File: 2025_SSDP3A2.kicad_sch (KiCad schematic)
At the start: 66 parts, among them J1 SolderPad, J2 SolderPad, J3 SolderPad, J4 SolderPad, Q1 CSD19534Q5A, Q2 BSC0805LS, U1 LM5146RGYR

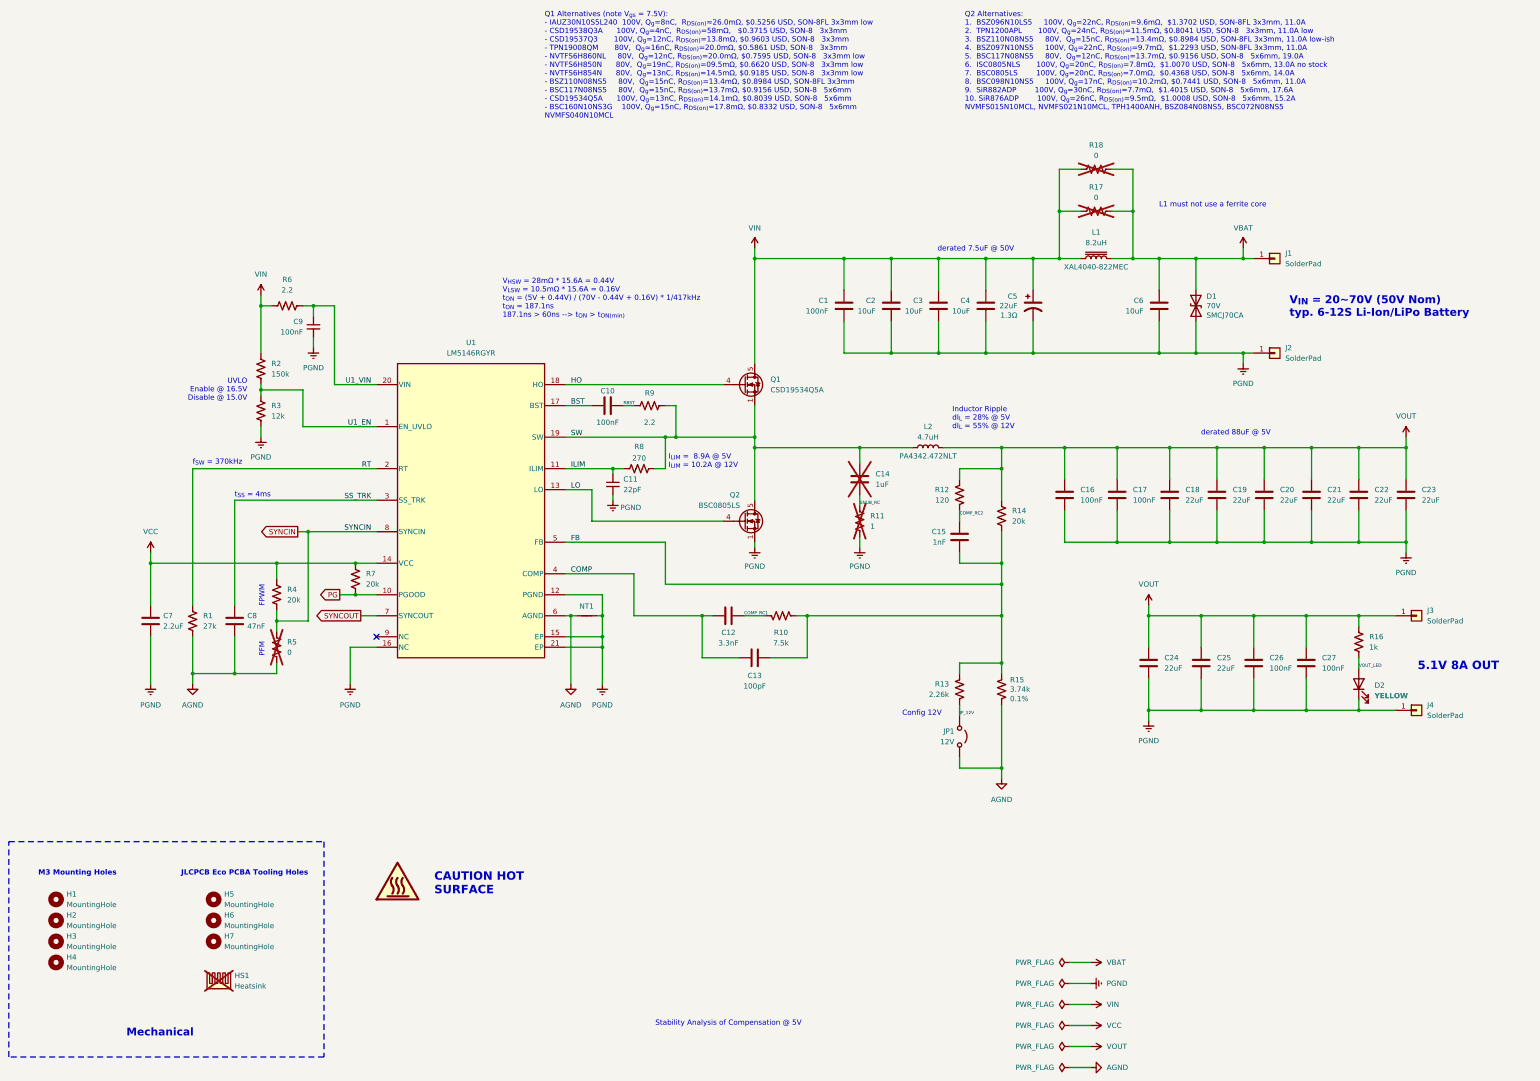
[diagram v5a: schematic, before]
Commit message: Revised PCB layout, simplified EMI filter
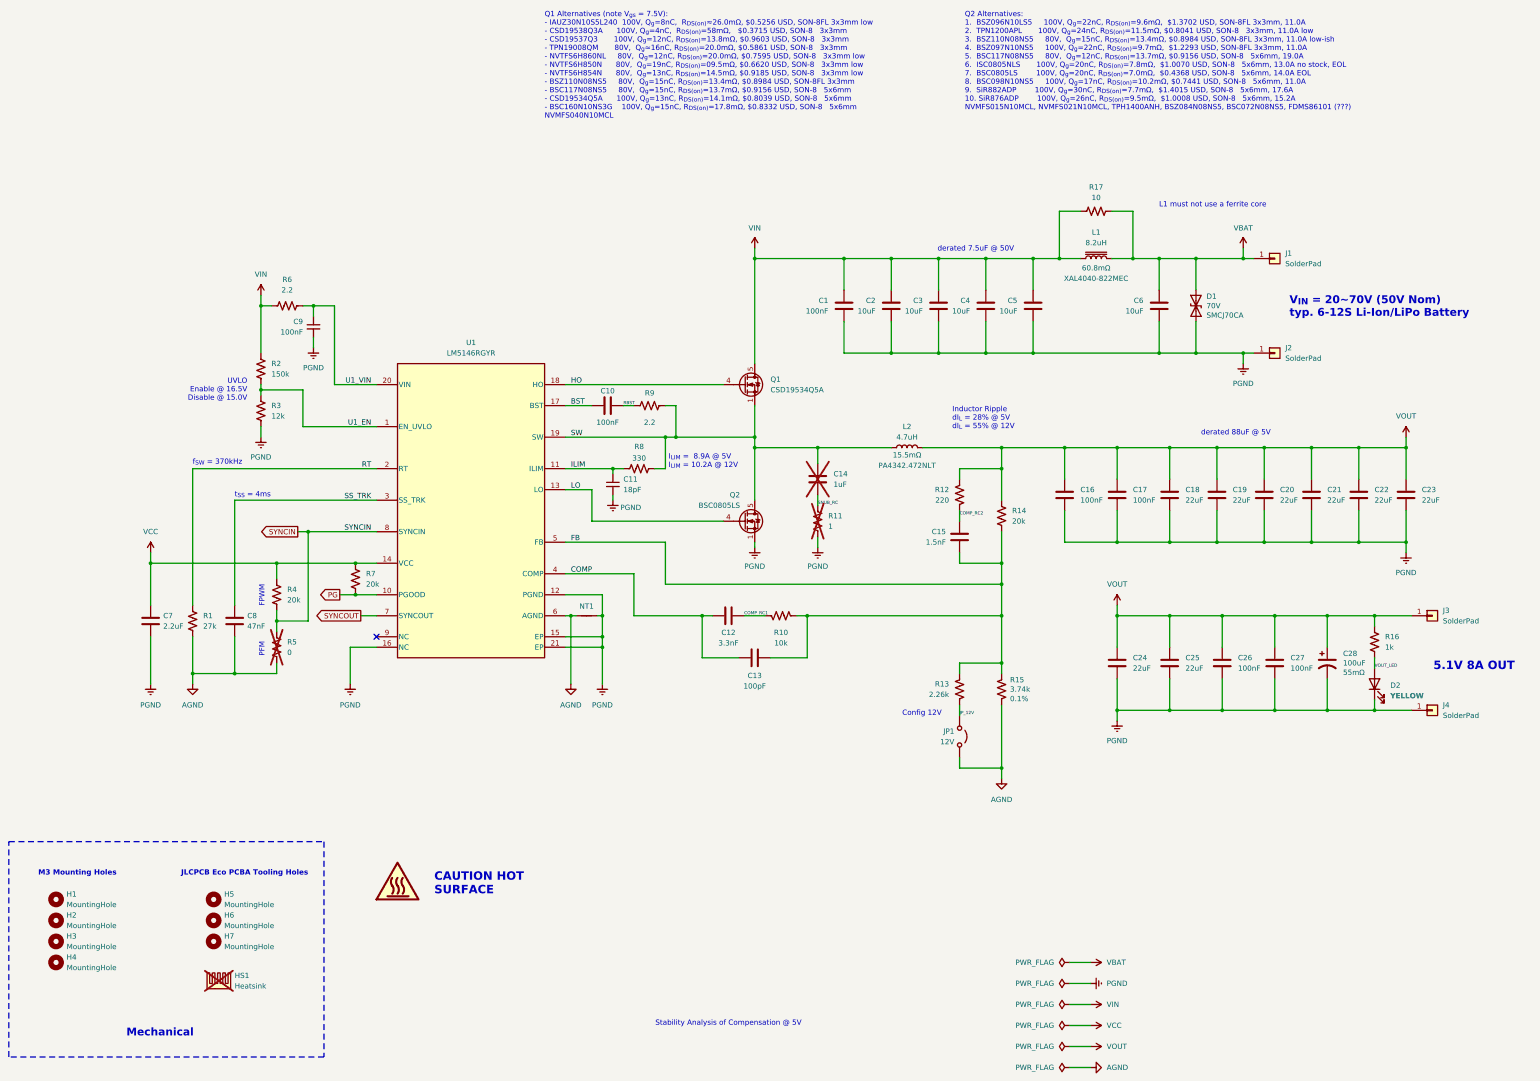
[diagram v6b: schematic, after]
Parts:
- removed C5: 22uF, Capacitor_SMD:CP_Elec_8x10.5, symbol Device:C_Polarized_US
- removed R18: 0, Resistor_SMD:R_2010_5025Metric, symbol Device:R_US
- added C28: 100uF, Capacitor_Tantalum_SMD:CP_EIA-7343-30_AVX-N_HandSolder, symbol Device:C_Polarized_US
- added C5: 10uF, Capacitor_SMD:C_1210_3225Metric, symbol Device:C
- C1, C10, C16, C17, C26, C27, C9: MANUFACTURER (none) -> YAGEO; Tolerance (none) -> 10%; Voltage (none) -> 100V
- C11: value 22pF -> 18pF; LCSC PN C408549 -> C913624; MANUFACTURER (none) -> Murata Electronics; Tolerance (none) -> 5%; Voltage (none) -> 100V
- C12, C7, C8: MANUFACTURER (none) -> Panasonic; Tolerance (none) -> 10%; Voltage (none) -> 50V
- C13: MANUFACTURER (none) -> Panasonic; Tolerance (none) -> 5%; Voltage (none) -> 50V
- C15: value 1nF -> 1.5nF; LCSC PN C1588 -> C1595; MANUFACTURER (none) -> Guangdong Fenghua; Part Type Basic -> Preferred Extended; Tolerance (none) -> 10%; Voltage (none) -> 50V
- C18, C19, C20, C21, C22, C23, C24, C25: ESR (none) -> 3.4mΩ; MANUFACTURER (none) -> Panasonic; Tolerance (none) -> 20%; Voltage (none) -> 25V
- C2, C3, C4, C6: ESR (none) -> 2mΩ; MANUFACTURER (none) -> Murata Electronics; Tolerance (none) -> 10%; Voltage (none) -> 100V
- D1: FT Rotation Offset (none) -> 0; LCSC PN (none) -> C41411746; MANUFACTURER (none) -> Zhuhai Hongjiacheng; Part Type (none) -> Preferred Extended; Voltage (none) -> 113V
- D2: MANUFACTURER (none) -> Hubei KENTO Electronics
- HS1: MANUFACTURER (none) -> Wakefield-Vette
- L1: ESR (none) -> 60.8mΩ; MANUFACTURER (none) -> Coilcraft; Tolerance (none) -> 20%
- L2: ESR (none) -> 15.5mΩ; MANUFACTURER (none) -> Pulse Electronics; Tolerance (none) -> 20%
- Q1: ESR (none) -> 13.8mΩ; FT Rotation Offset 270 -> 0; MANUFACTURER (none) -> Texas Instruments; Voltage (none) -> 100V
- Q2: ESR (none) -> 7.1mΩ; FT Rotation Offset 270 -> 0; MANUFACTURER (none) -> Infineon Technologies; Voltage (none) -> 100V
- R1, R14, R2, R3, R4, R6, R7, R9: MANUFACTURER (none) -> UNI-ROYAL; Power (none) -> 0.1W; Tolerance (none) -> 1%; Voltage (none) -> 75V
- R10: value 7.5k -> 10k; LCSC PN C23234 -> C25804; MANUFACTURER (none) -> UNI-ROYAL; Power (none) -> 0.1W; Tolerance (none) -> 1%; Voltage (none) -> 75V
- R12: value 120 -> 220; LCSC PN C22787 -> C22962; MANUFACTURER (none) -> UNI-ROYAL; Power (none) -> 0.1W; Tolerance (none) -> 1%; Voltage (none) -> 75V
- R13: MANUFACTURER (none) -> Guangdong Fenghua; Power (none) -> 0.1W; Tolerance (none) -> 1%; Voltage (none) -> 50V
- R15: MANUFACTURER (none) -> YAGEO; Power (none) -> 0.1W; Voltage (none) -> 75V
- R16: MANUFACTURER (none) -> UNI-ROYAL; Power (none) -> 0.125W; Tolerance (none) -> 1%; Voltage (none) -> 150V
- R17: value 0 -> 10; footprint Resistor_SMD:R_2010_5025Metric -> Resistor_SMD:R_1210_3225Metric_Pad1.30x2.65mm_HandSolder; FT Rotation Offset (none) -> 0; LCSC PN (none) -> C17903; MANUFACTURER (none) -> UNI-ROYAL; Part Type (none) -> Basic; Power (none) -> 0.25W; Tolerance (none) -> 1%; now fitted; now in the parts list
- R8: value 270 -> 330; LCSC PN C22966 -> C23138; MANUFACTURER (none) -> UNI-ROYAL; Power (none) -> 0.1W; Tolerance (none) -> 1%; Voltage (none) -> 75V
- U1: MANUFACTURER (none) -> Texas Instruments; Voltage (none) -> 100V
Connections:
- net PGND: now also C28.2, C5.2
- net VIN: now also C5.1
- net VOUT: now also C28.1
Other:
- note removed: "V_{HSW} = 28mΩ * 15.6A = 0.44V V_{LSW} = 10.5mΩ * 15.6A = 0.16V t_{ON} = (5V + 0.44V) / (70V - 0.44V + 0.16V) * 1/417kHz t_{ON} = 187.1ns 187.1ns > 60ns --> t_{ON} > t_{ON(min)}"
- moved on the sheet: C14, C24, C25, C26, C27, D2, J3, J4, L2, R11, R16

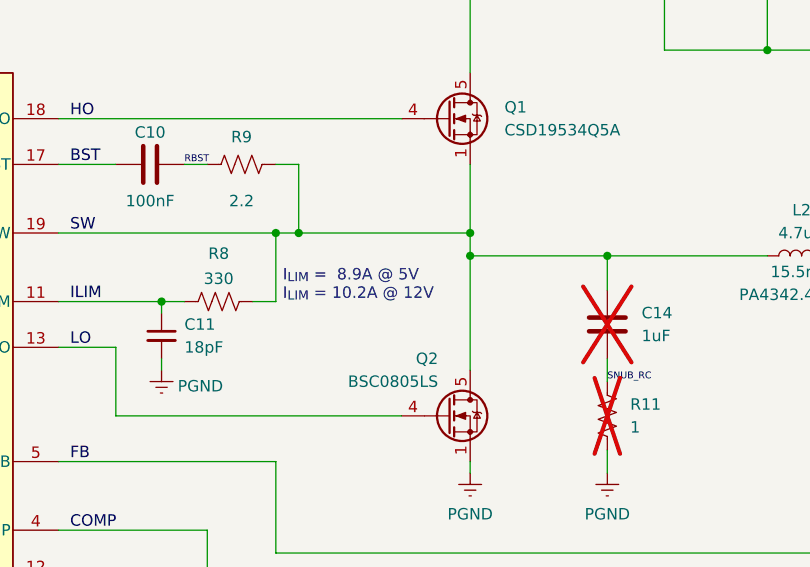
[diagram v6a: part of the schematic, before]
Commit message: Updated ILIM values
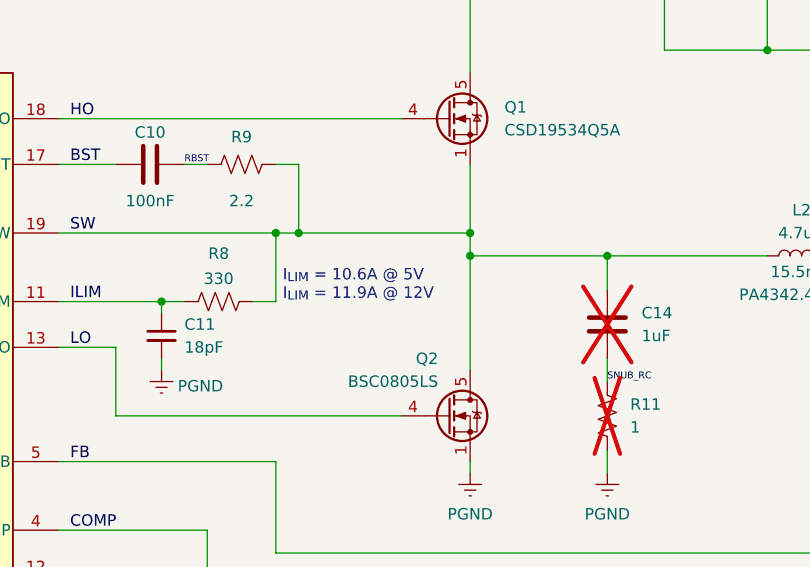
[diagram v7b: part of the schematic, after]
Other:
- note added: "I_{LIM} = 10.6A @ 5V I_{LIM} = 11.9A @ 12V"
- note removed: "I_{LIM} = 8.9A @ 5V I_{LIM} = 10.2A @ 12V"
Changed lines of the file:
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@@
 		)
 	)
-	(text "I_{LIM} =  8.9A @ 5V\nI_{LIM} = 10.2A @ 12V"
+	(text "I_{LIM} = 10.6A @ 5V\nI_{LIM} = 11.9A @ 12V"
 		(exclude_from_sim no)
 		(at 182.372 134.112 0)

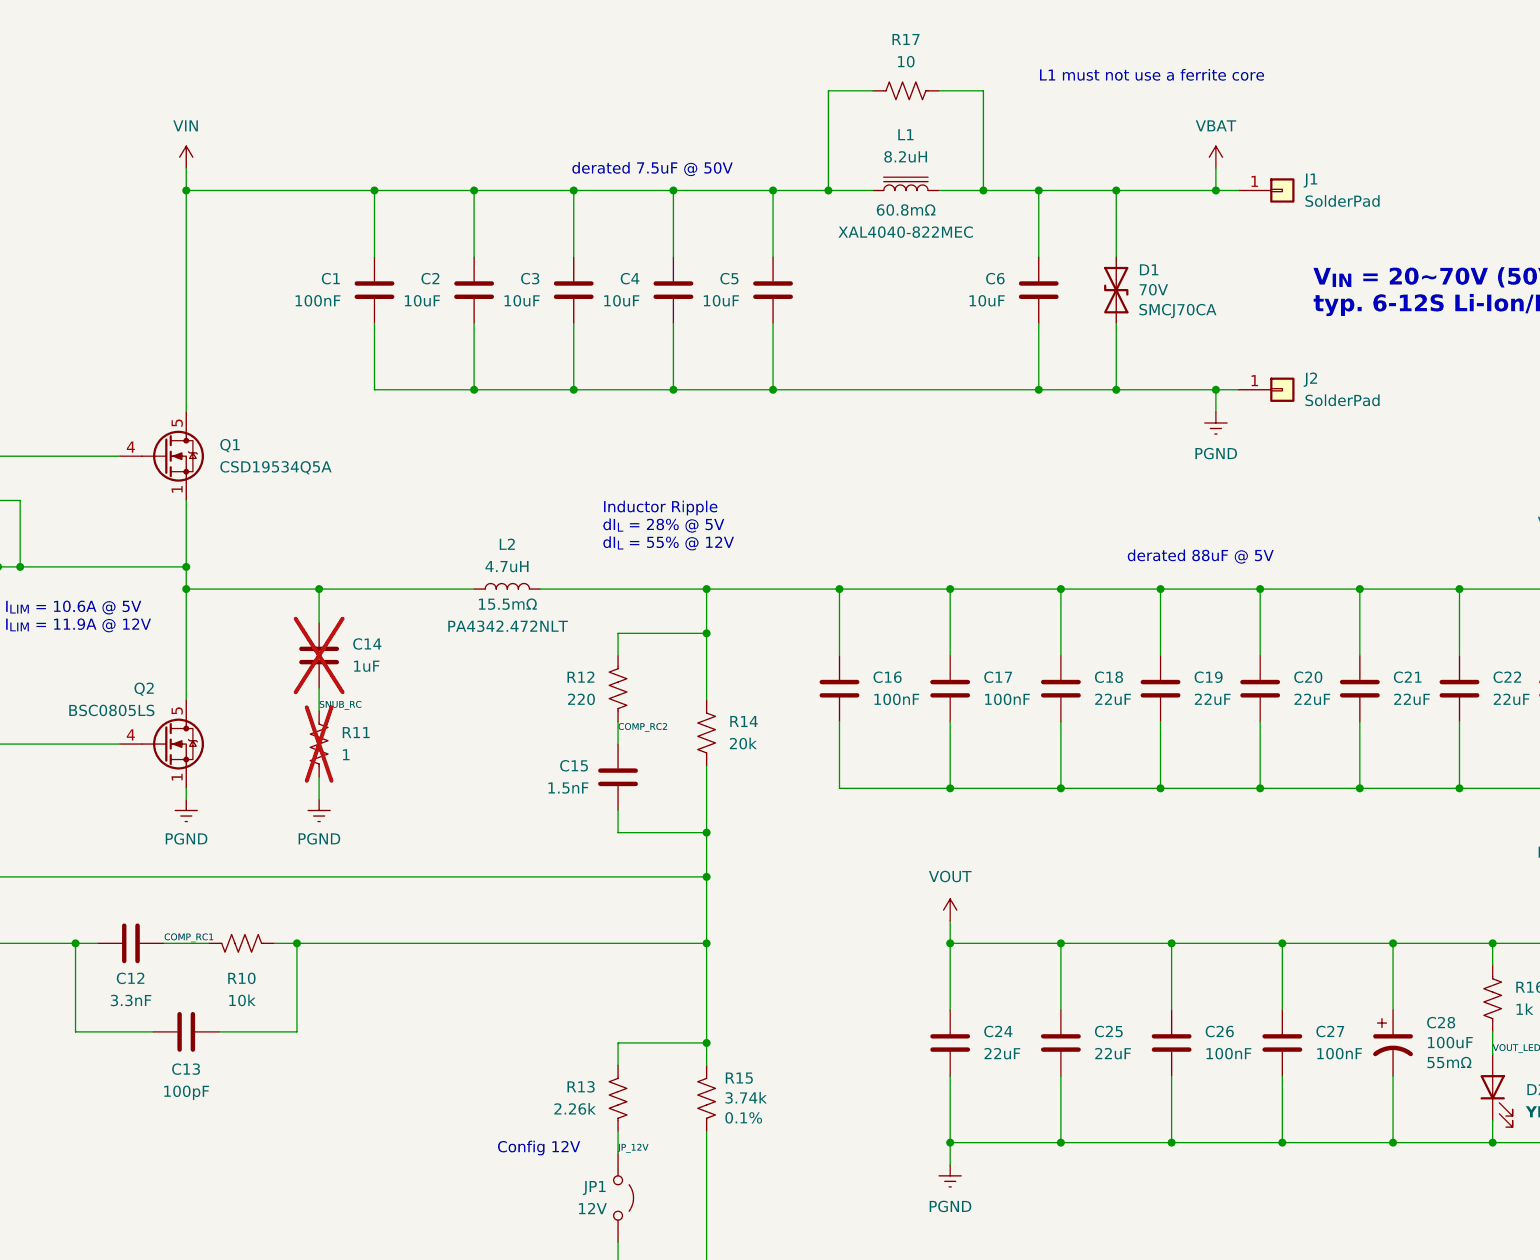
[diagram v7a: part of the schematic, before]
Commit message: Revised simulations, revised compensation network
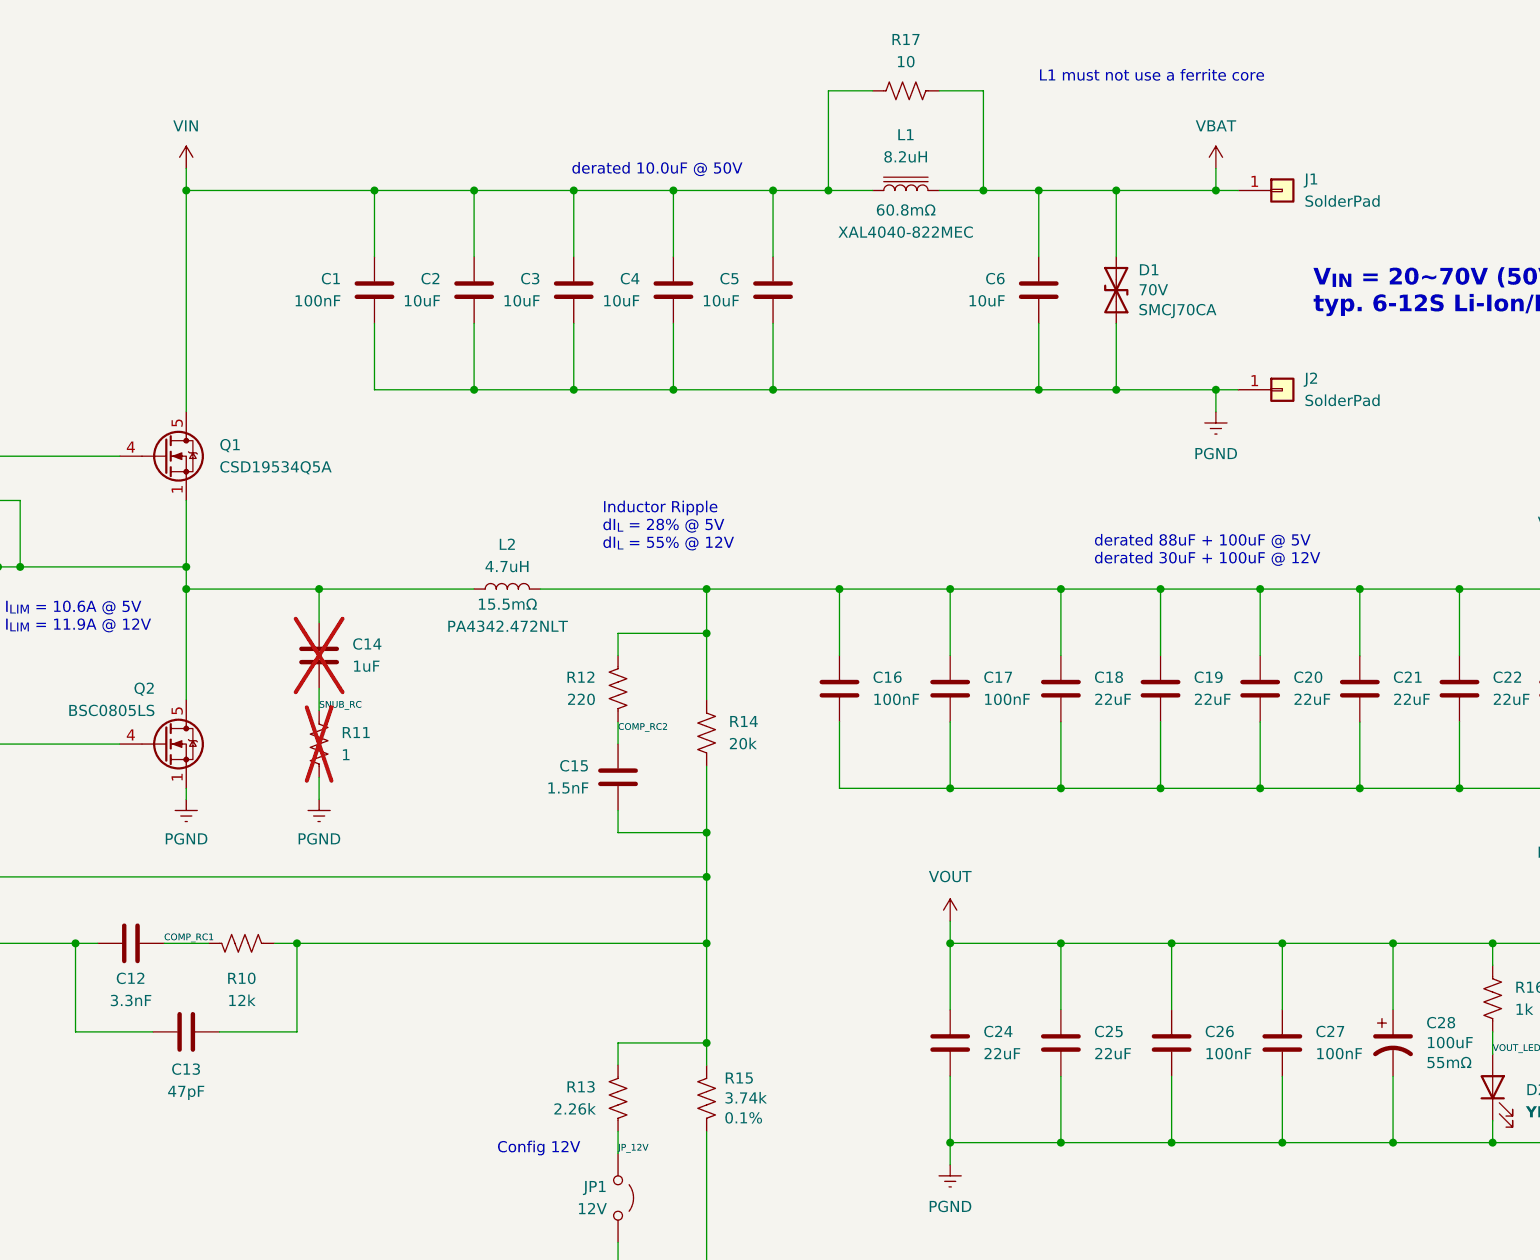
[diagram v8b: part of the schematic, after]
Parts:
- C13: value 100pF -> 47pF; LCSC PN C14858 -> C1671
- R10: value 10k -> 12k; LCSC PN C25804 -> C22790
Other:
- note added: "derated 10.0uF @ 50V"
- note added: "derated 88uF + 100uF @ 5V derated 30uF + 100uF @ 12V"
- note removed: "derated 7.5uF @ 50V"
- note removed: "derated 88uF @ 5V"
